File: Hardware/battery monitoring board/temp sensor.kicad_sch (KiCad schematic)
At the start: 1 part, among them U1 MAX31855KASA

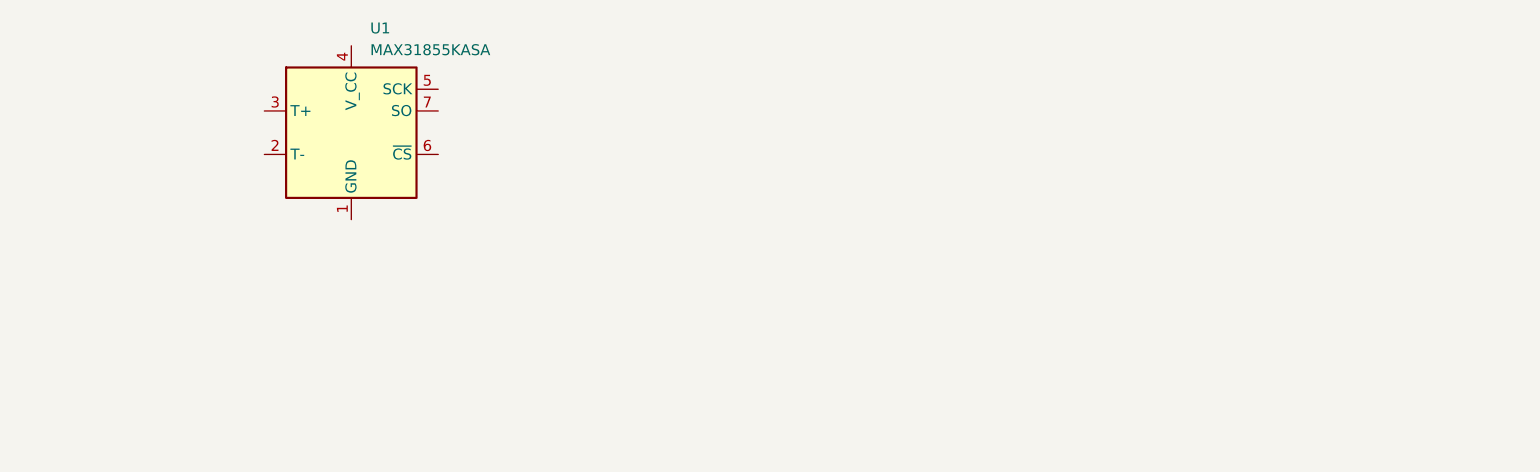
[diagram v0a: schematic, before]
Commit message: added back wiped battery monitoring board
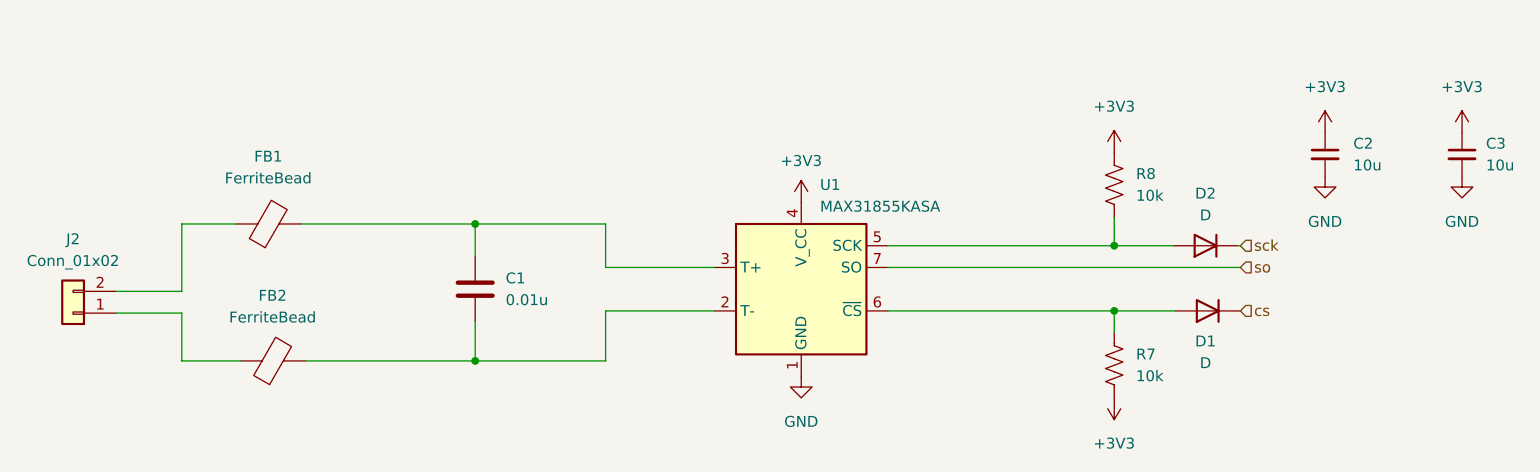
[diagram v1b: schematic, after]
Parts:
- added C1: 0.01u, symbol Device:C
- added C2, C3: 10u, symbol Device:C_Small
- added D1, D2: D, symbol Device:D
- added FB1, FB2: FerriteBead, symbol Device:FerriteBead
- added J2: Conn_01x02, 4ms_Connector:Pins_1x02_2.54mm_TH, symbol PCM_4ms_Connector:Conn_01x02
- added R7, R8: 10k, symbol Device:R_US
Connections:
- net GND: now reaches U1.1 (GND)
- net GND: now also C2.2, C3.2
- net at U1.2 (T-): now also C1.2, FB2.2
- net at U1.3 (T+): now also C1.1, FB1.2
- net +3V3: now reaches U1.4 (V_CC)
- net +3V3: now also C2.1, C3.1, R7.2, R8.1
- net at U1.5 (SCK): now also D2.2 (A), R8.2
- net at U1.6 (~{CS}): now also D1.2 (A), R7.1
- net so: now reaches U1.7 (SO)
- new net: FB1.1, J2.2 (Pin_2)
- new net: FB2.1, J2.1 (Pin_1)
- new net cs: D1.1 (K)
- new net sck: D2.1 (K)
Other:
- moved on the sheet: U1

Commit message: Revert "Merge branch 'hardware' of https://github.com/bruin-underwater-robotics/2023-2024 into hardware"
This reverts commit 1d5f0f31a35e539c7b0b2eac7ff2db3bf82506a7, reversing
changes made to b9b3862216192341382b87943b4a1d0c2c46b631.
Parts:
- removed C1: 0.01u, symbol Device:C
- removed C2, C3: 10u, symbol Device:C_Small
- removed D1, D2: D, symbol Device:D
- removed FB1, FB2: FerriteBead, symbol Device:FerriteBead
- removed J2: Conn_01x02, 4ms_Connector:Pins_1x02_2.54mm_TH, symbol PCM_4ms_Connector:Conn_01x02
- removed R7, R8: 10k, symbol Device:R_US
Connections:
- net +3V3: no longer names the net of U1.4 (V_CC)
- net GND: no longer names the net of U1.1 (GND)
- net so: no longer names the net of U1.7 (SO)
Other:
- moved on the sheet: U1
